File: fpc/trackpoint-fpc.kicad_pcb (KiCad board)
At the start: 2 copper layers, 37 x 22.1 mm, 2 parts, among them P1 CONN_8, P2 CONN_5

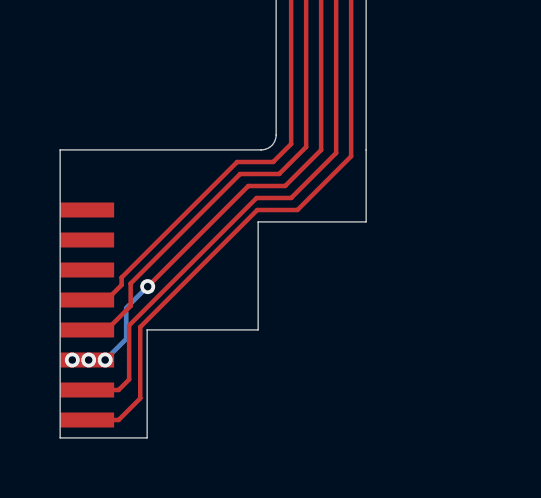
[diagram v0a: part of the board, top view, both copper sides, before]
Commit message: Add another 8x0.5 footprint to the other side.
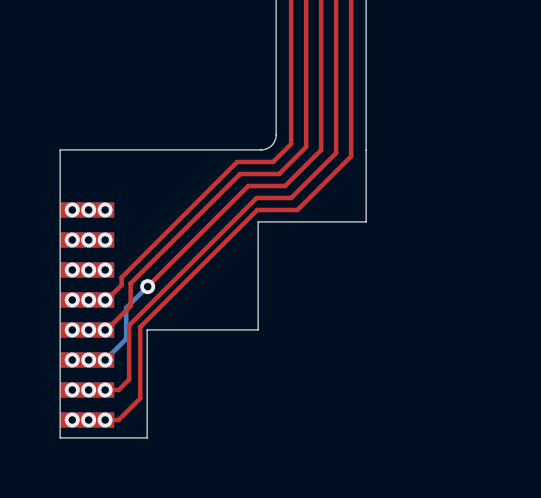
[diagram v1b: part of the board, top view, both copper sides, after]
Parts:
- added P3: CONN_8, UGL:Trackpoint_FPC_8x1_pads, B.Cu at (190.5, 145.2)
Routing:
- net /CLK: track 18.9 -> 17.4 mm, vias 0 -> 3
- net /VCC: track 24.8 -> 23.4 mm, vias 0 -> 3
- net /GND: track 23.5 -> 22.1 mm, vias 0 -> 3
- net /RESET: track 20.2 -> 19.1 mm
- net /DATA: track 17.0 -> 16.4 mm, vias 0 -> 3
- net /RBTN: vias 0 -> 3
- net /MBTN: vias 0 -> 3
- net /LBTN: vias 0 -> 3
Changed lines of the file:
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@@
     (thickness 1.6)
     (drawings 73)
-    (tracks 87)
+    (tracks 101)
     (zones 0)
-    (modules 2)
+    (modules 3)
     (nets 9)
   )
@@
     (pad 1 smd rect (at -3.5 0 270) (size 0.5 1.8) (layers F.Cu F.Paste F.Mask)
       (net 8 /LBTN))
+  )
+  (module UGL:Trackpoint_FPC_8x1_pads (layer B.Cu)
+    (at 190.5 145.2 270)
+    (attr smd)
+    (fp_text reference P3 (at 0 -2.05 270) (layer B.SilkS) hide
+      (effects (font (size 1 1) (thickness 0.15)) (justify mirror))
+    )
+    (fp_text value CONN_8 (at 0 -3.2 270) (layer B.Fab)
+      (effects (font (size 1 1) (thickness 0.15)) (justify mirror))
+    )
+    (pad 1 smd rect (at -3.5 0 270) (size 0.5 1.8) (layers B.Cu B.Paste B.Mask)
+      (net 8 /LBTN))
+    (pad 2 smd rect (at -2.5 0 270) (size 0.5 1.8) (layers B.Cu B.Paste B.Mask)
+      (net 7 /MBTN))
+    (pad 3 smd rect (at -1.5 0 270) (size 0.5 1.8) (layers B.Cu B.Paste B.Mask)
+      (net 6 /RBTN))
+    (pad 4 smd rect (at -0.5 0 270) (size 0.5 1.8) (layers B.Cu B.Paste B.Mask)
+      (net 5 /DATA))
+    (pad 5 smd rect (at 0.5 0 270) (size 0.5 1.8) (layers B.Cu B.Paste B.Mask)
+      (net 4 /CLK))
+    (pad 6 smd rect (at 1.5 0 270) (size 0.5 1.8) (layers B.Cu B.Paste B.Mask)
+      (net 3 /RESET))
+    (pad 7 smd rect (at 2.5 0 270) (size 0.5 1.8) (layers B.Cu B.Paste B.Mask)
+      (net 2 /GND))
+    (pad 8 smd rect (at 3.5 0 270) (size 0.5 1.8) (layers B.Cu B.Paste B.Mask)
+      (net 1 /VCC))
   )
   (gr_line (start 223.6 148.952743) (end 223.6 140.377107) (angle 90) (layer Edge.Cuts) (width 0.01))
@@
   (segment (start 219.6 135.5) (end 219.6 148.7) (width 0.5) (layer B.Cu) (net 0))
   (segment (start 215.6 135.5) (end 215.6 148.7) (width 0.5) (layer B.Cu) (net 0))
-  (segment (start 190.5 148.7) (end 191.3 148.7) (width 0.2032) (layer F.Cu) (net 1))
   (segment (start 199.3 139.912139) (end 199.3 132.35) (width 0.15) (layer F.Cu) (net 1))
   (segment (start 197.512139 141.7) (end 199.3 139.912139) (width 0.15) (layer F.Cu) (net 1))
@@
   (segment (start 191.55 148.7) (end 192.26999 147.98001) (width 0.15) (layer F.Cu) (net 1))
   (segment (start 199.3 132.35) (end 199.3 129.7) (width 0.15) (layer F.Cu) (net 1))
-  (segment (start 190.5 148.7) (end 191.55 148.7) (width 0.15) (layer F.Cu) (net 1))
-  (segment (start 190.5 147.7) (end 191.3 147.7) (width 0.2032) (layer F.Cu) (net 2))
+  (via (at 190.005 148.7) (size 0.5) (drill 0.25) (layers F.Cu B.Cu) (net 1))
+  (via (at 191.1 148.7) (size 0.5) (drill 0.25) (layers F.Cu B.Cu) (net 1))
+  (via (at 190.55 148.7) (size 0.5) (drill 0.25) (layers F.Cu B.Cu) (net 1))
+  (segment (start 191.55 148.7) (end 191.1 148.7) (width 0.15) (layer F.Cu) (net 1))
   (segment (start 198.8 132.35) (end 198.8 129.7) (width 0.15) (layer F.Cu) (net 2))
   (segment (start 197.3 141.3) (end 198.8 139.8) (width 0.15) (layer F.Cu) (net 2))
-  (segment (start 190.5 147.7) (end 191.55 147.7) (width 0.15) (layer F.Cu) (net 2))
   (segment (start 198.8 139.8) (end 198.8 132.35) (width 0.15) (layer F.Cu) (net 2))
   (segment (start 191.899991 145.547947) (end 196.147938 141.3) (width 0.15) (layer F.Cu) (net 2))
@@
   (segment (start 191.899991 147.350009) (end 191.899991 145.547947) (width 0.15) (layer F.Cu) (net 2))
   (segment (start 196.147938 141.3) (end 197.3 141.3) (width 0.15) (layer F.Cu) (net 2))
+  (via (at 190.005 147.7) (size 0.5) (drill 0.25) (layers F.Cu B.Cu) (net 2))
+  (via (at 190.55 147.7) (size 0.5) (drill 0.25) (layers F.Cu B.Cu) (net 2))
+  (via (at 191.1 147.7) (size 0.5) (drill 0.25) (layers F.Cu B.Cu) (net 2))
+  (segment (start 191.55 147.7) (end 191.1 147.7) (width 0.15) (layer F.Cu) (net 2))
   (via (at 190.005 146.7) (size 0.5) (drill 0.25) (layers F.Cu B.Cu) (net 3))
-  (segment (start 190.5 146.7) (end 190.005 146.7) (width 0.15) (layer F.Cu) (net 3))
   (via (at 190.55 146.7) (size 0.5) (drill 0.25) (layers F.Cu B.Cu) (net 3))
   (segment (start 190.5 146.7) (end 190.6 146.7) (width 0.15) (layer F.Cu) (net 3))
   (via (at 191.1 146.7) (size 0.5) (drill 0.25) (layers F.Cu B.Cu) (net 3))
-  (segment (start 190.5 146.7) (end 191.1 146.7) (width 0.15) (layer F.Cu) (net 3))
   (via (at 192.517942 144.253825) (size 0.5) (drill 0.25) (layers F.Cu B.Cu) (net 3))
   (segment (start 198.3 139.7) (end 198.3 131.4) (width 0.15) (layer F.Cu) (net 3))
@@
   (segment (start 191.8 146) (end 191.8 144.971767) (width 0.15) (layer B.Cu) (net 3))
   (segment (start 191.1 146.7) (end 191.8 146) (width 0.15) (layer B.Cu) (net 3))
-  (segment (start 190.5 145.7) (end 191.3 145.7) (width 0.15) (layer F.Cu) (net 4))
   (segment (start 197.8 139.6) (end 197.8 131.8) (width 0.15) (layer F.Cu) (net 4))
   (segment (start 196.9 140.5) (end 197.8 139.6) (width 0.15) (layer F.Cu) (net 4))
@@
   (segment (start 191.950011 144.149989) (end 195.6 140.5) (width 0.15) (layer F.Cu) (net 4))
   (segment (start 191.15 145.7) (end 191.950011 144.899989) (width 0.15) (layer F.Cu) (net 4))
-  (segment (start 190.5 145.7) (end 191.15 145.7) (width 0.15) (layer F.Cu) (net 4))
+  (via (at 190.005 145.7) (size 0.5) (drill 0.25) (layers F.Cu B.Cu) (net 4))
+  (via (at 190.55 145.7) (size 0.5) (drill 0.25) (layers F.Cu B.Cu) (net 4))
+  (via (at 191.1 145.7) (size 0.5) (drill 0.25) (layers F.Cu B.Cu) (net 4))
   (segment (start 197.3 139.5) (end 197.3 131.6) (width 0.15) (layer F.Cu) (net 5))
   (segment (start 195.5 140.1) (end 196.7 140.1) (width 0.15) (layer F.Cu) (net 5))
@@
   (segment (start 191.15 144.7) (end 191.65 144.2) (width 0.15) (layer F.Cu) (net 5))
   (segment (start 196.7 140.1) (end 197.3 139.5) (width 0.15) (layer F.Cu) (net 5))
-  (segment (start 190.5 144.7) (end 191.15 144.7) (width 0.15) (layer F.Cu) (net 5))
+  (via (at 190.005 144.7) (size 0.5) (drill 0.25) (layers F.Cu B.Cu) (net 5))
+  (via (at 190.55 144.7) (size 0.5) (drill 0.25) (layers F.Cu B.Cu) (net 5))
+  (via (at 191.1 144.7) (size 0.5) (drill 0.25) (layers F.Cu B.Cu) (net 5))
+  (via (at 190.005 143.7) (size 0.5) (drill 0.25) (layers F.Cu B.Cu) (net 6))
+  (via (at 190.55 143.7) (size 0.5) (drill 0.25) (layers F.Cu B.Cu) (net 6))
+  (via (at 191.1 143.7) (size 0.5) (drill 0.25) (layers F.Cu B.Cu) (net 6))
+  (via (at 190.005 142.7) (size 0.5) (drill 0.25) (layers F.Cu B.Cu) (net 7))
+  (via (at 190.55 142.7) (size 0.5) (drill 0.25) (layers F.Cu B.Cu) (net 7))
+  (via (at 191.1 142.7) (size 0.5) (drill 0.25) (layers F.Cu B.Cu) (net 7))
+  (via (at 190.005 141.7) (size 0.5) (drill 0.25) (layers F.Cu B.Cu) (net 8))
+  (via (at 190.55 141.7) (size 0.5) (drill 0.25) (layers F.Cu B.Cu) (net 8))
+  (via (at 191.1 141.7) (size 0.5) (drill 0.25) (layers F.Cu B.Cu) (net 8))
 )

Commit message: Update 5x0.5 pads.
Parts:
- moved P2 1.25 mm to (198.3, 128.4)
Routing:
- net /CLK: track 17.4 -> 19.9 mm
- net /DATA: track 16.4 -> 18.7 mm
- net /RESET: track 19.1 -> 21.1 mm
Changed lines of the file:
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@@
   )
   (module UGL:Trackpoint_FPC_5x0.5_pads (layer F.Cu)
-    (at 198.3 129.7)
+    (at 198.3 128.45)
     (attr smd)
     (fp_text reference P2 (at 0 3.65) (layer F.SilkS) hide
@@
       (effects (font (size 1 1) (thickness 0.15)))
     )
-    (pad 1 smd rect (at -1 0) (size 0.3 5) (layers F.Cu F.Paste F.Mask)
+    (pad 5 smd rect (at 1 0) (size 0.3 2.5) (layers F.Cu F.Paste F.Mask)
+      (net 1 /VCC))
+    (pad 4 smd rect (at 0.5 0) (size 0.3 2.5) (layers F.Cu F.Paste F.Mask)
+      (net 2 /GND))
+    (pad 3 smd rect (at 0 0) (size 0.3 2.5) (layers F.Cu F.Paste F.Mask)
+      (net 3 /RESET))
+    (pad 2 smd rect (at -0.5 0) (size 0.3 2.5) (layers F.Cu F.Paste F.Mask)
+      (net 4 /CLK))
+    (pad 1 smd rect (at -1 0) (size 0.3 2.5) (layers F.Cu F.Paste F.Mask)
       (net 5 /DATA))
-    (pad 2 smd rect (at -0.5 0) (size 0.3 5) (layers F.Cu F.Paste F.Mask)
-      (net 4 /CLK))
-    (pad 3 smd rect (at 0 0) (size 0.3 5) (layers F.Cu F.Paste F.Mask)
-      (net 3 /RESET))
-    (pad 4 smd rect (at 0.5 0) (size 0.3 5) (layers F.Cu F.Paste F.Mask)
-      (net 2 /GND))
-    (pad 5 smd rect (at 1 0) (size 0.3 5) (layers F.Cu F.Paste F.Mask)
-      (net 1 /VCC))
   )
   (module UGL:Trackpoint_FPC_8x1_pads locked (layer F.Cu)
@@
   (via (at 191.1 146.7) (size 0.5) (drill 0.25) (layers F.Cu B.Cu) (net 3))
   (via (at 192.517942 144.253825) (size 0.5) (drill 0.25) (layers F.Cu B.Cu) (net 3))
-  (segment (start 198.3 139.7) (end 198.3 131.4) (width 0.15) (layer F.Cu) (net 3))
   (segment (start 197.1 140.9) (end 198.3 139.7) (width 0.15) (layer F.Cu) (net 3))
   (segment (start 195.871767 140.9) (end 197.1 140.9) (width 0.15) (layer F.Cu) (net 3))
@@
   (segment (start 191.8 146) (end 191.8 144.971767) (width 0.15) (layer B.Cu) (net 3))
   (segment (start 191.1 146.7) (end 191.8 146) (width 0.15) (layer B.Cu) (net 3))
-  (segment (start 197.8 139.6) (end 197.8 131.8) (width 0.15) (layer F.Cu) (net 4))
+  (segment (start 198.3 139.7) (end 198.3 129.4) (width 0.15) (layer F.Cu) (net 3))
   (segment (start 196.9 140.5) (end 197.8 139.6) (width 0.15) (layer F.Cu) (net 4))
   (segment (start 195.6 140.5) (end 196.9 140.5) (width 0.15) (layer F.Cu) (net 4))
@@
   (via (at 190.55 145.7) (size 0.5) (drill 0.25) (layers F.Cu B.Cu) (net 4))
   (via (at 191.1 145.7) (size 0.5) (drill 0.25) (layers F.Cu B.Cu) (net 4))
-  (segment (start 197.3 139.5) (end 197.3 131.6) (width 0.15) (layer F.Cu) (net 5))
+  (segment (start 197.8 139.6) (end 197.8 129.3) (width 0.15) (layer F.Cu) (net 4))
   (segment (start 195.5 140.1) (end 196.7 140.1) (width 0.15) (layer F.Cu) (net 5))
   (segment (start 191.65 143.95) (end 195.5 140.1) (width 0.15) (layer F.Cu) (net 5))
@@
   (via (at 190.55 144.7) (size 0.5) (drill 0.25) (layers F.Cu B.Cu) (net 5))
   (via (at 191.1 144.7) (size 0.5) (drill 0.25) (layers F.Cu B.Cu) (net 5))
+  (segment (start 197.3 139.5) (end 197.3 129.3) (width 0.15) (layer F.Cu) (net 5))
   (via (at 190.005 143.7) (size 0.5) (drill 0.25) (layers F.Cu B.Cu) (net 6))
   (via (at 190.55 143.7) (size 0.5) (drill 0.25) (layers F.Cu B.Cu) (net 6))
